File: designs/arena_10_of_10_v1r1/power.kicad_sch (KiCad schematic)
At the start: 4 parts, among them J25 Barrel_Jack, J26 Barrel_Jack, SW1 SW_SPDT, U82 RB-XXYYD

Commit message: Work on layout and routing.
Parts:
- J25, J26: footprint arena_custom:DCJACK_2PIN_HIGHCURRENT -> arena_custom:DC-053D-20A
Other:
- note added: "Change DC Jack to PN DC-053D-20A Korean Hroparts Elec LCSC C707274"
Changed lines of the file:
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@@
 	(generator_version "9.0")
 	(paper "A4")
+	(text "Change DC Jack to\nPN DC-053D-20A Korean Hroparts Elec \nLCSC C707274\n"
+		(exclude_from_sim no)
+		(at 76.708 50.292 0)
+		(effects
+			(font
+				(size 1.27 1.27)
+			)
+		)
+	)
 	(text "External power supply"
 		(exclude_from_sim no)
@@
 			)
 		)
-		(property "Footprint" "arena_custom:DCJACK_2PIN_HIGHCURRENT"
+		(property "Footprint" "arena_custom:DC-053D-20A"
 			(at 76.2 69.596 0)
 			(effects
@@
 			)
 		)
-		(property "Footprint" "arena_custom:DCJACK_2PIN_HIGHCURRENT"
+		(property "Footprint" "arena_custom:DC-053D-20A"
 			(at 76.2 32.766 0)
 			(effects

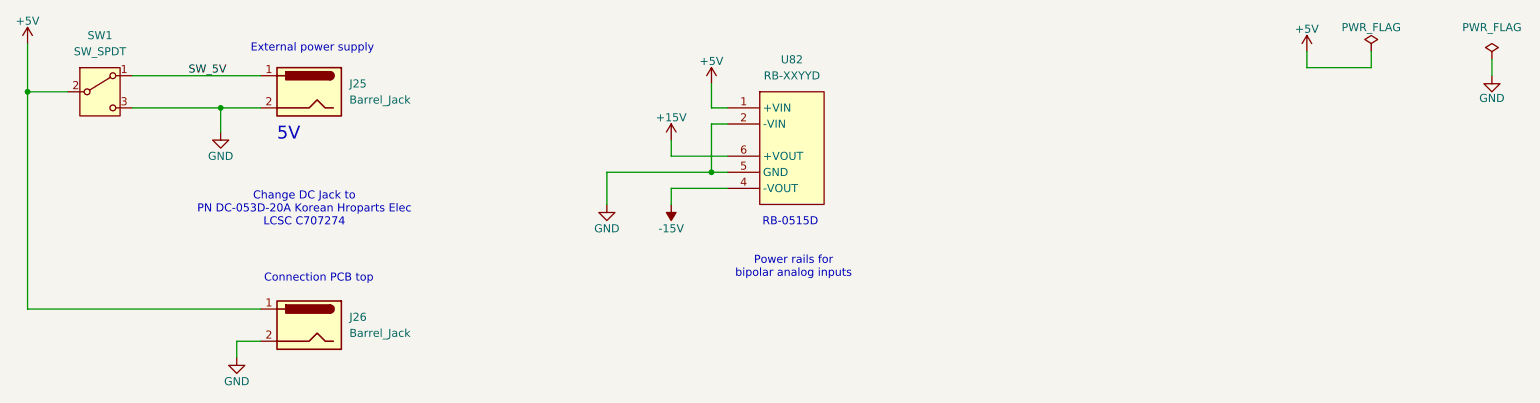
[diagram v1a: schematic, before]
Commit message: Added LCSC part numbers to Symbol Fields Table.
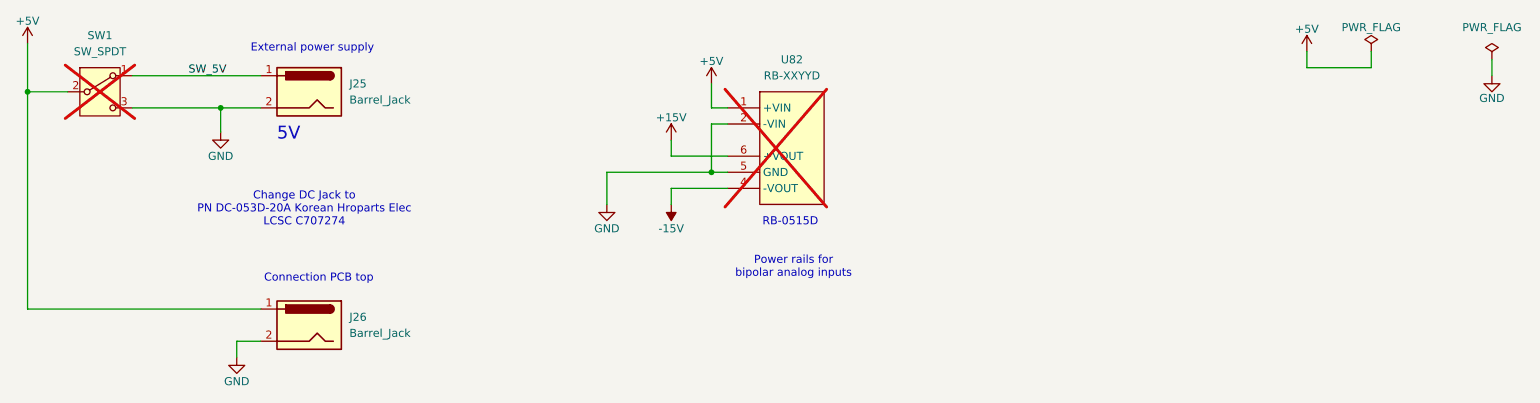
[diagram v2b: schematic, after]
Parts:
- J25, J26: LCSC Part # (none) -> C707274
- SW1, U82: now not fitted; now left out of the parts list
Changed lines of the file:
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@@
+			)
+		)
+		(property "LCSC Part #" "C707274"
+			(at 77.47 68.58 0)
+			(effects
+				(font
+					(size 1.27 1.27)
+				)
+				(hide yes)
 			)
 		)
@@
 			)
 		)
+		(property "LCSC Part #" "C707274"
+			(at 77.47 31.75 0)
+			(effects
+				(font
+					(size 1.27 1.27)
+				)
+				(hide yes)
+			)
+		)
 		(pin "1"
 		)
@@
 		(unit 1)
 		(exclude_from_sim no)
-		(in_bom yes)
-		(on_board yes)
-		(dnp no)
+		(in_bom no)
+		(on_board yes)
+		(dnp yes)
 		(property "Reference" "U82"
 			(at 153.67 26.67 0)
@@
 		(unit 1)
 		(exclude_from_sim no)
-		(in_bom yes)
-		(on_board yes)
-		(dnp no)
+		(in_bom no)
+		(on_board yes)
+		(dnp yes)
 		(fields_autoplaced yes)
 		(property "Reference" "SW1"

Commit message: Added silkscreens.  Added required FT Rotations/Offsets for JLCPCB.
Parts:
- J25, J26: FT Position Offset (none) -> 0,-1.143
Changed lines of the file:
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@@
+			)
+		)
+		(property "FT Position Offset" "0,-1.143"
+			(at 77.47 68.58 0)
+			(effects
+				(font
+					(size 1.27 1.27)
+				)
+				(hide yes)
 			)
 		)
@@
 			(at 77.47 31.75 0)
 			(effects
+				(font
+					(size 1.27 1.27)
+				)
+				(hide yes)
+			)
+		)
+		(property "FT Position Offset" "0,-1.143"
+			(at 77.47 31.75 0)
+			(effects
